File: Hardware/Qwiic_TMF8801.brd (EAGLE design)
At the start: 25.4 x 25.4 mm, 27 parts, among them J1 QWIIC_RIGHT_ANGLE, J2 QWIIC_RIGHT_ANGLE, U1 TMF8801

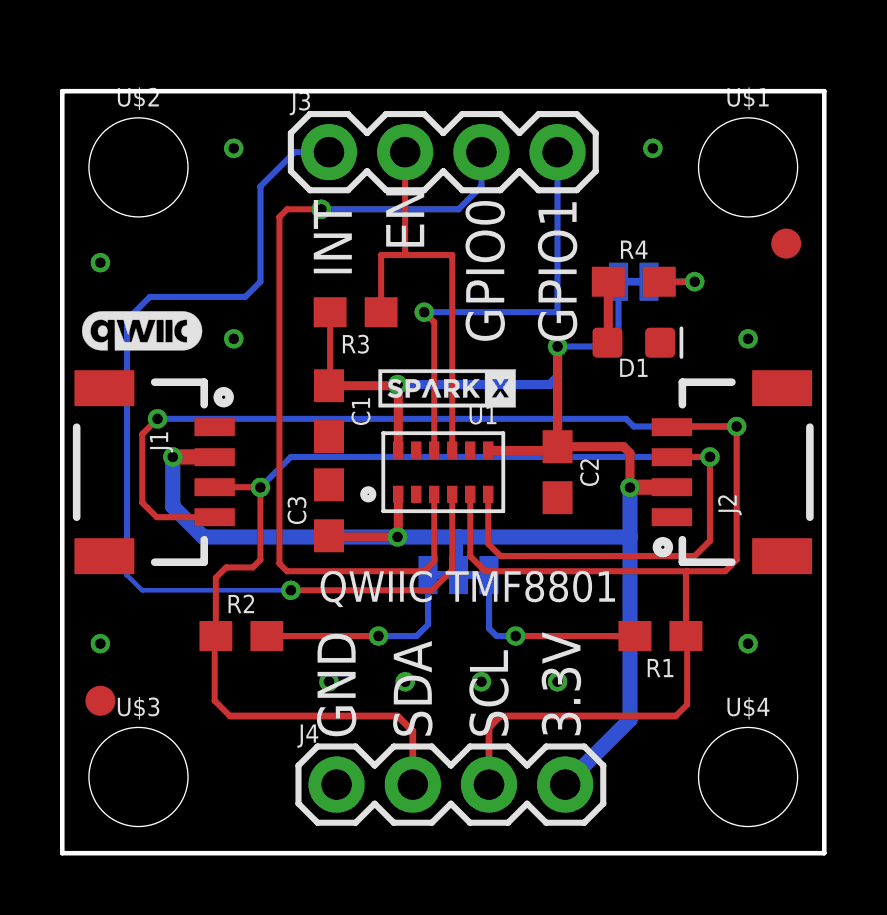
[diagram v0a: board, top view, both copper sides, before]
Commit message: Add files via upload
Added missing libraries and labels; changed design per Nathan's feedback and SparfFun design guidelines
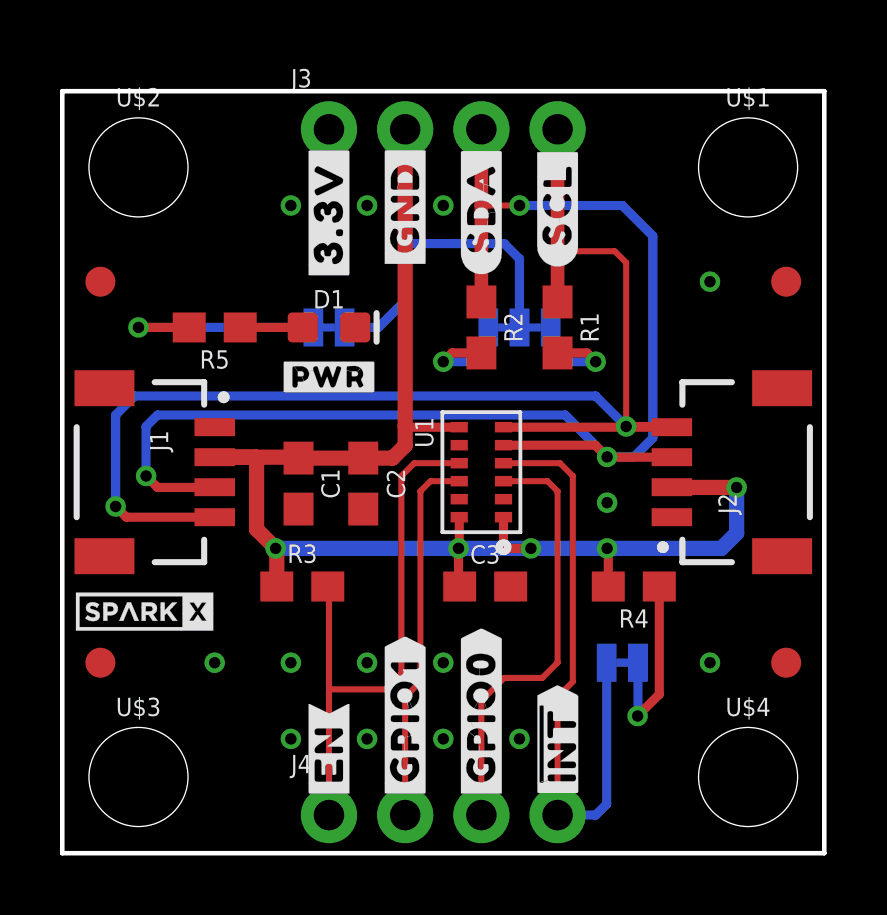
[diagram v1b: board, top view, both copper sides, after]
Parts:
- removed U$41: (no value), SparkFun-Aesthetics:QWIIC_4MM
- added FD3, FD4: FIDUCIAL1X2, SparkFun-Aesthetics:FIDUCIAL-1X2
- added JP3: JUMPER-SMT_2_NC_TRACE_SILK, SparkFun-Jumpers:SMT-JUMPER_2_NC_TRACE_SILK
- added R5: 1k, SparkFun-Resistors:0603
- added U$10, U$26: (no value), output:#GPIO1#7
- added U$11, U$23: (no value), output:#EN#6
- added U$12: (no value), output:#PWR#88019
- added U$13: (no value), output:##INT#_PULLUP#88020
- added U$14: (no value), output:#I2C_PULLUP#88022
- added U$17, U$5: (no value), output:#3#3V#1
- added U$18, U$7: (no value), output:#GND#0
- added U$19, U$6: (no value), output:#SDA#4
- added U$21, U$22: (no value), output:#SCL#5
- added U$24, U$8: (no value), output:##INT##7
- added U$25, U$9: (no value), output:#GPIO0#7
- J1, J2: device SparkFun-Connectors:1X04_1MM_RA -> SparkFun-Connectors:JST04_1MM_RA
- J3, J4: device SparkFun-Connectors:1X04 -> SparkFun-Connectors:1X04_NO_SILK
- R4: value 1k -> 10k
- U$15: device output:#LED#2712 -> output:#LED_EN#88021
- U$16: device output:#I�C#2714 -> output:TIME#OF#FLIGHT_TMF88018
- moved FD1 22.9 mm to (1.27, 19.1)
- moved U$15 13.8 mm to (5.21, 17.5)
- moved R2 13.0 mm to (14.0, 17.5), turned to 270 degrees
- moved JP2 12.7 mm to (18.7, 6.35)
- moved U$20 12.5 mm to (2.74, 8.05)
- moved R1 10.8 mm to (16.5, 17.5), turned to 270 degrees
- moved D1 10.2 mm to (8.89, 17.5)
- moved R4 10.2 mm to (19.1, 8.89), turned to 180 degrees
- moved R3 9.32 mm to (8.00, 8.89)
- moved JP1 8.50 mm to (15.2, 17.5)
- moved C2 6.49 mm to (10.0, 12.3)
- moved C3 5.79 mm to (14.1, 8.89), turned to 0 degrees
- moved U$16 3.45 mm to (12.8, 14.4)
- moved U$27 3.43 mm to (12.7, 12.1)
- moved C1 2.62 mm to (7.87, 12.3)
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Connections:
- removed net INT: J3.1, U1.4
- new net !INT: J4.4, JP2.2, U1.4
- new net N$5: JP2.1, R4.1
- net 3.3V: now also J3.2, JP3.2, R4.2; no longer J4.4, JP2.2
- net EN: now also J4.1; no longer J3.2
- net GND: now also J3.1; no longer J4.1
- net GPIO0: now also J4.3; no longer J3.3
- net GPIO1: now also J4.2; no longer J3.4
- net N$1: now also R5.1; no longer R4.1
- net N$4: now also JP3.1, R5.2; no longer JP2.1, R4.2
- net SCL: now also J3.4, U1.6; no longer J4.3, U1.5
- net SDA: now also J3.3, U1.5; no longer J4.2, U1.6
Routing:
- net INT: track 33.3 -> 0.00 mm, vias 1 -> 0
- net !INT: track 0.00 -> 20.5 mm
- net GPIO0: track 27.5 -> 14.5 mm, vias 1 -> 0
- net SCL: track 56.3 -> 45.1 mm
- net N$5: track 0.00 -> 6.40 mm, vias 0 -> 1
- net N$4: track 2.71 -> 7.52 mm
- net EN: track 14.2 -> 19.0 mm
- net N$3: track 7.18 -> 3.90 mm
- net N$2: track 6.75 -> 3.90 mm
- net GPIO1: track 14.5 -> 12.4 mm, vias 1 -> 0
- net 3.3V: track 62.8 -> 64.4 mm
- net SDA: track 47.5 -> 46.4 mm, vias 2 -> 3
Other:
- board text removed: "3.3V"
- board text removed: "EN"
- board text removed: "GND"
- board text removed: "GPIO0"
- board text removed: "GPIO1"
- board text removed: "INT"
- board text removed: "QWIIC TMF8801"
- board text removed: "SCL"
- board text removed: "SDA"
